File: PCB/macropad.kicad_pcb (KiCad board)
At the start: 2 copper layers, 80.5 x 95.5 mm, 36 parts, among them SW1 Kailh Choc V2, SW10 Kailh Choc V2, SW11 Kailh Choc V2, SW12 Kailh Choc V2, SW13 Kailh Choc V2, SW14 Kailh Choc V2, SW15 Kailh Choc V2, SW16 Kailh Choc V2, SW2 Kailh Choc V2, SW3 Kailh Choc V2, SW4 Kailh Choc V2, SW5 Kailh Choc V2, SW6 Kailh Choc V2, SW7 Kailh Choc V2, SW8 Kailh Choc V2, SW9 Kailh Choc V2, U2 SEEEDUINO XIAO RP2040

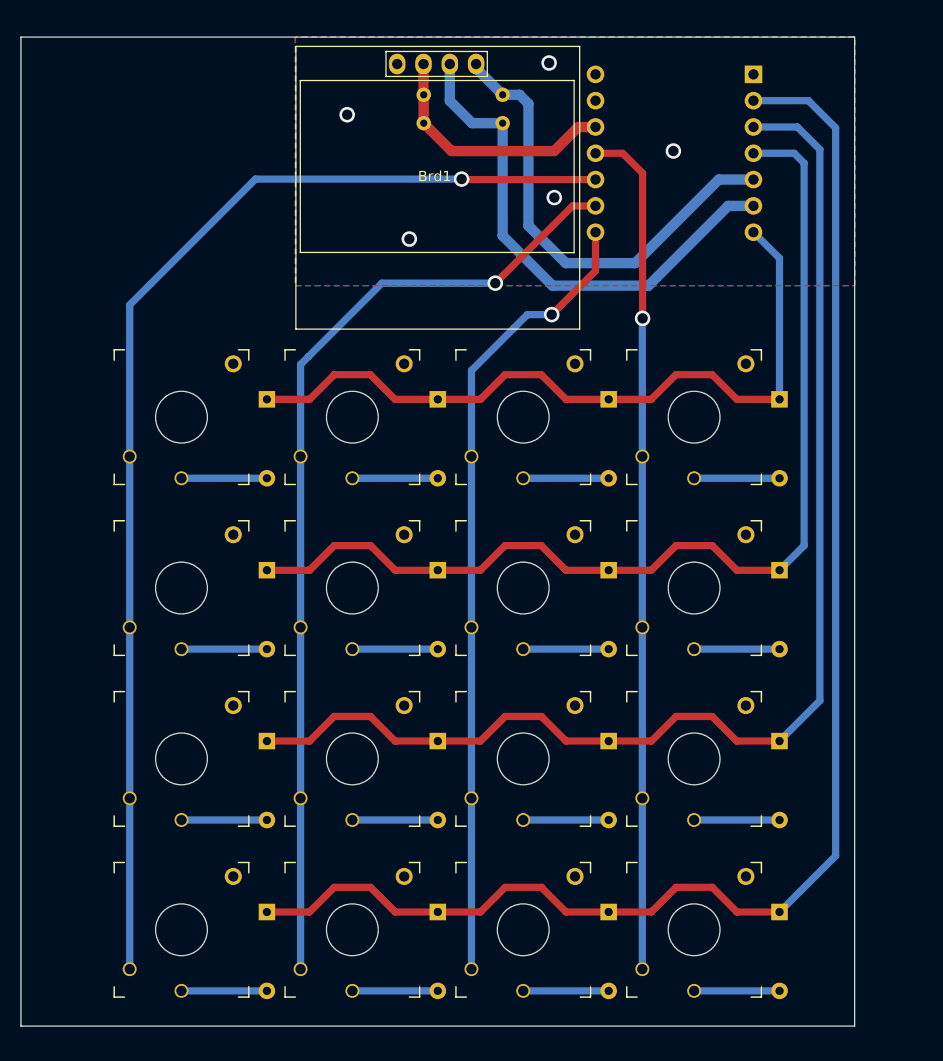
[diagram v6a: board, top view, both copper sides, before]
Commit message: Revamped switch footprints and routing
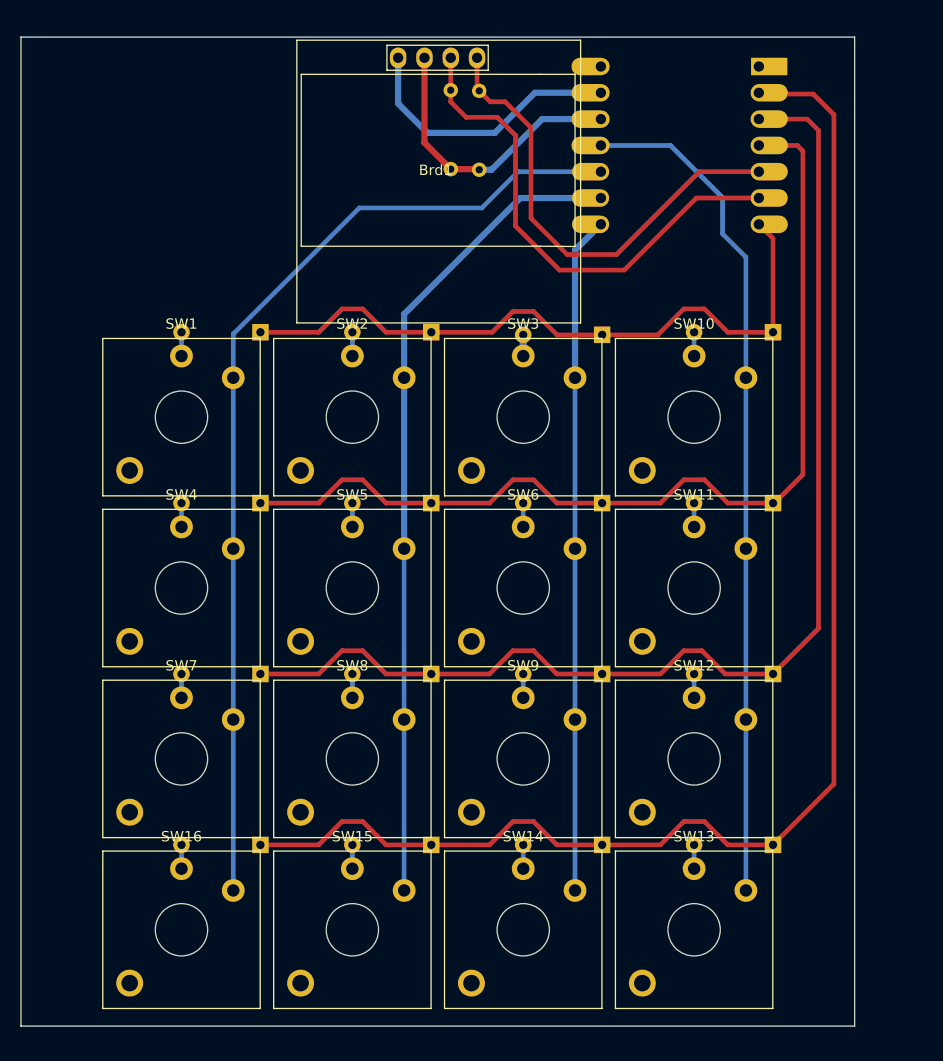
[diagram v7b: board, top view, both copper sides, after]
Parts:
- SW1, SW10, SW11, SW12, SW13, SW14, SW15, SW16, SW2, SW3, SW4, SW5, SW6, SW7, SW8, SW9: footprint key:SW_Kailh_Choc_V2_THT -> key:SW_Kailh_Choc_V2
- U2: footprint seed:XIAO-Generic-Thruhole-14P-2.54-21X17.8MM -> seed:XIAO-Generic-Hybrid-14P-2.54-21X17.8MM
- moved R2 9.01 mm to (148.8, 62.8), turned to 90 degrees
- moved D1 6.51 mm to (127.6, 78.5), turned to 180 degrees
- moved D10 6.51 mm to (177.1, 78.5), turned to 180 degrees
- moved D11 6.51 mm to (177.1, 95.0), turned to 180 degrees
- moved D12 6.51 mm to (177.1, 111.5), turned to 180 degrees
- moved D2 6.51 mm to (144.1, 78.5), turned to 180 degrees
- moved D4 6.51 mm to (127.6, 95.0), turned to 180 degrees
- moved D5 6.51 mm to (144.1, 95.0), turned to 180 degrees
- moved D6 6.51 mm to (160.6, 95.0), turned to 180 degrees
- moved D7 6.51 mm to (127.6, 111.5), turned to 180 degrees
- moved D8 6.51 mm to (144.1, 111.5), turned to 180 degrees
- moved D9 6.51 mm to (160.6, 111.5), turned to 180 degrees
- moved D13 6.51 mm to (177.1, 128.0), turned to 180 degrees
- moved D14 6.51 mm to (160.6, 128.0), turned to 180 degrees
- moved D15 6.51 mm to (144.1, 128.0), turned to 180 degrees
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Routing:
- net GND: track 0.00 -> 26.8 mm, vias 5 -> 0
- net COL0: track 114.2 -> 95.7 mm, vias 1 -> 0
- net COL1: track 93.2 -> 79.3 mm, vias 1 -> 0
- net COL2: track 77.5 -> 65.4 mm, vias 1 -> 0
- net ROW0: track 72.6 -> 66.1 mm
- net ROW3: track 142.4 -> 136.2 mm
- net Net-(D3-A): track 8.25 -> 2.05 mm
- net ROW1: track 101.4 -> 95.2 mm
- net Net-(D9-A): track 8.25 -> 2.30 mm
- net Net-(D8-A): track 8.25 -> 2.30 mm
- net Net-(D7-A): track 8.25 -> 2.30 mm
- net Net-(D6-A): track 8.25 -> 2.30 mm
- net Net-(D5-A): track 8.25 -> 2.30 mm
- net Net-(D4-A): track 8.25 -> 2.30 mm
- net Net-(D2-A): track 8.25 -> 2.30 mm
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- removed copper zone on B.Cu, net GND
- removed copper zone on F.Cu, net GND
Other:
- board text added: "Rev 5.0"
- board text added: "Why so many revs :("
- board text removed: "Rev 4.0"

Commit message: Add LEDs to PCB
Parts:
- added D19: WS2812B, LED_SMD:LED_WS2812B_PLCC4_5.0x5.0mm_P3.2mm, F.Cu at (123.0, 72.2)
- added D20: WS2812B, LED_SMD:LED_WS2812B_PLCC4_5.0x5.0mm_P3.2mm, F.Cu at (169.8, 72.5)
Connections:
- U2 pad 1: unconnected-(U2-PA02_A0_D0-Pad1) -> COL3
- U2 pad 11: COL3 -> LED
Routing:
- net +5V: track 0.00 -> 76.7 mm, vias 0 -> 3
- net GND: track 26.8 -> 78.3 mm, vias 0 -> 3
- net Net-(D19-DIN): track 0.00 -> 43.3 mm
- net LED: track 0.00 -> 22.4 mm, vias 0 -> 1
- net COL1: track 79.3 -> 81.1 mm
- net COL0: track 95.7 -> 96.3 mm
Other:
- board text added: "Rev 5.1"
- board text removed: "Rev 5.0"
